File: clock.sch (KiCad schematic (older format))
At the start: 20 parts, among them SW2 SW_Push, SW3 SW_SPDT, U38 LM555xN, U39 74LS04, U40 74LS08, U41 74LS32, U42 LM555xN, U43 LM555xN

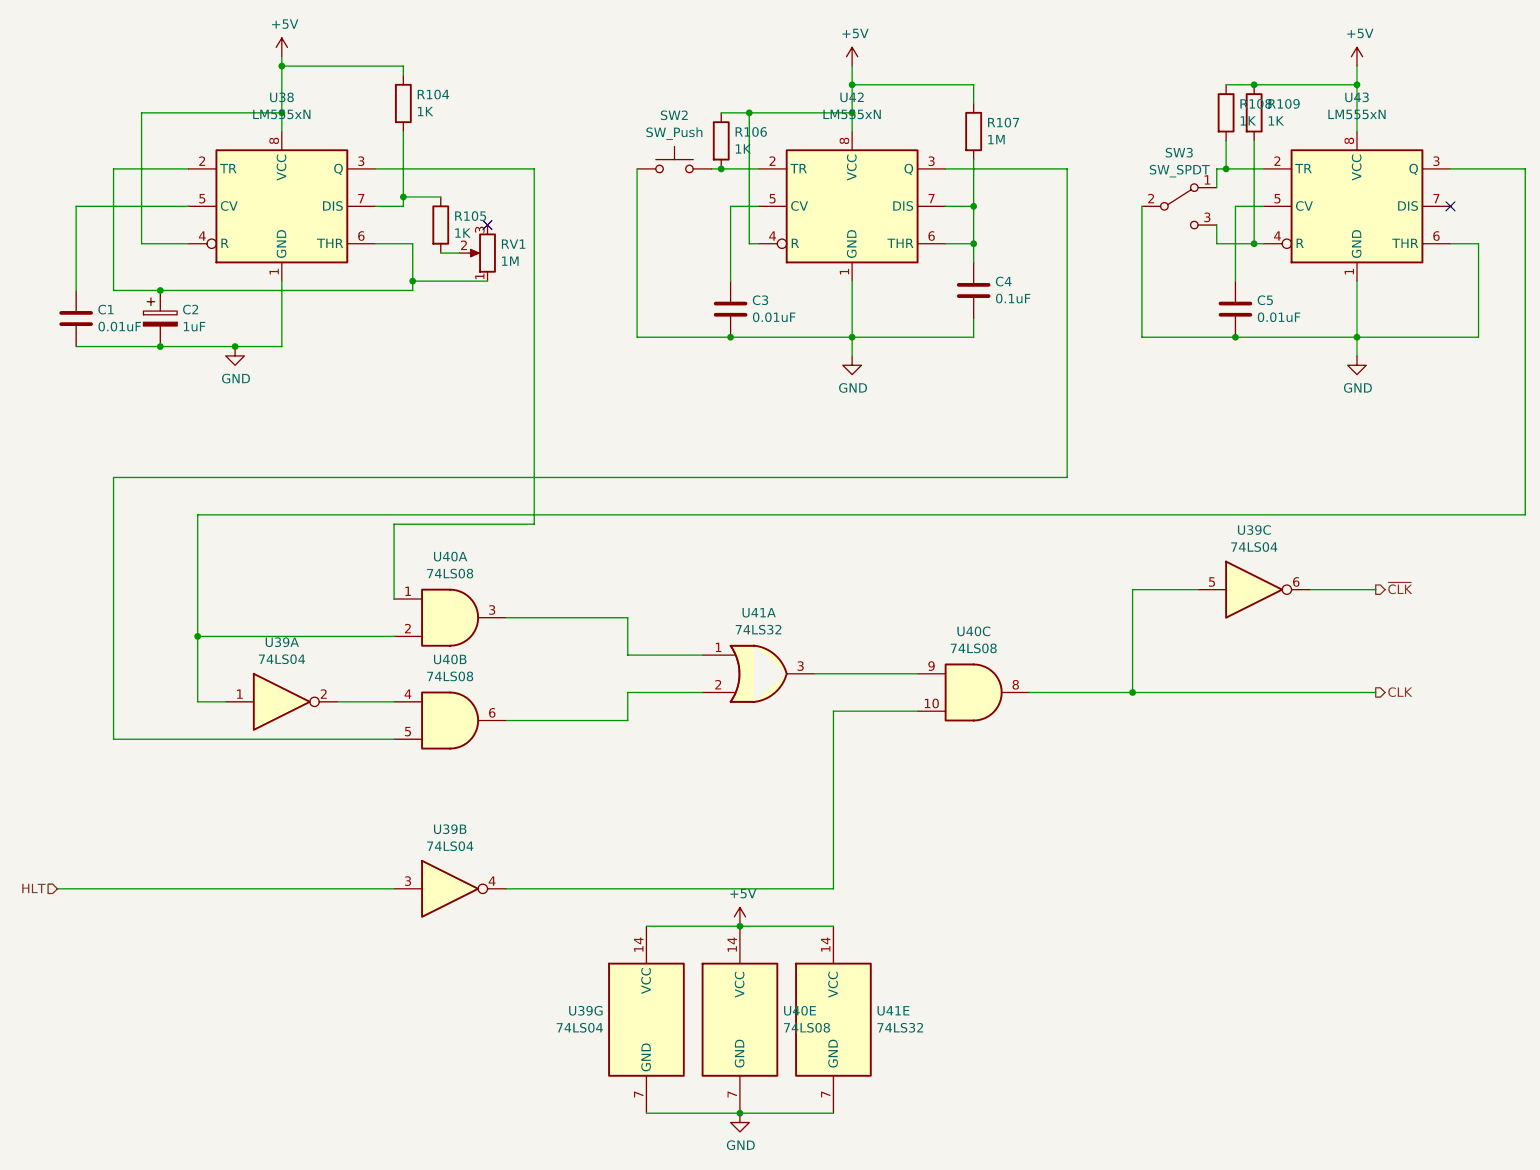
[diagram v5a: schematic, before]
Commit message: added timer.lib and using correct 555 timer
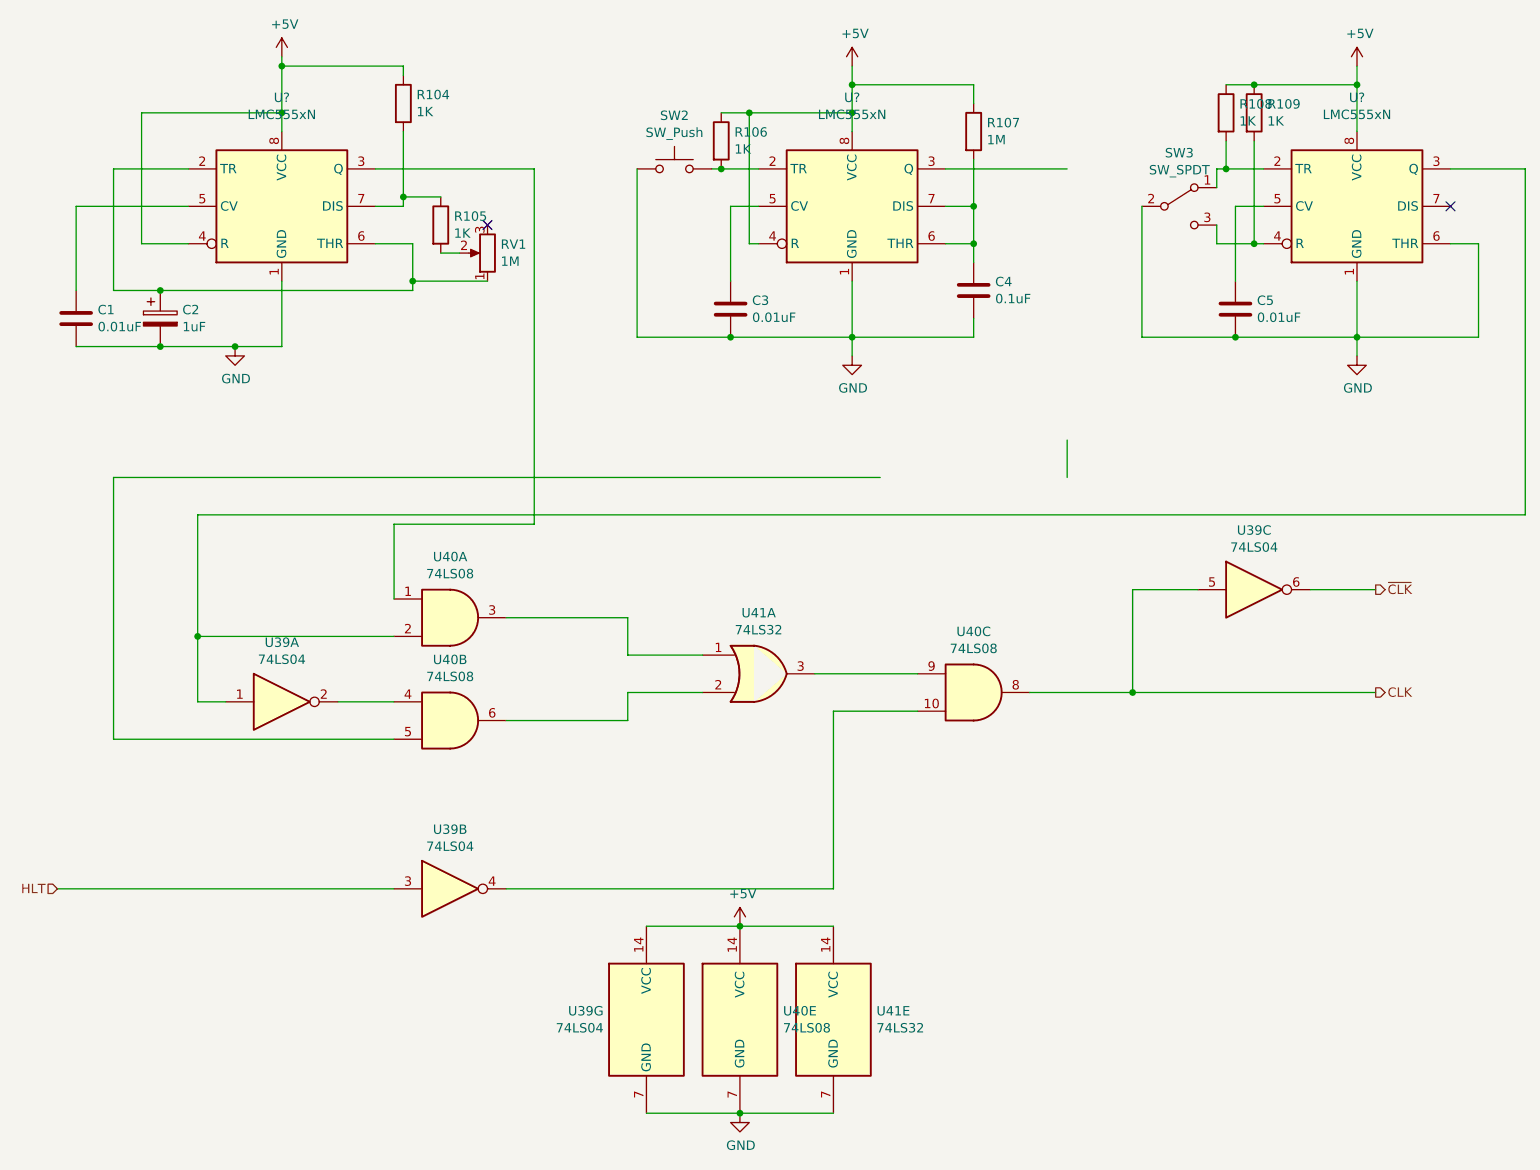
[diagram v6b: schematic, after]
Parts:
- removed U38, U42, U43: LM555xN, Package_DIP:DIP-8_W7.62mm, symbol 16bitCpu-rescue:LM555xN-Timer
- added U? (x3): LMC555xN, Package_DIP:DIP-8_W7.62mm, symbol Timer:LMC555xN
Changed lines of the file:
@@
 $Descr A4 11693 8268
 encoding utf-8
-Sheet 13 21
+Sheet 12 21
 Title ""
 Date ""
@@
 	9350 1700 9350 3550
 Wire Wire Line
-	9350 3550 2250 3550
-Wire Wire Line
 	2250 3550 2250 4200
 Wire Wire Line
@@
 	1800 4750 1800 3350
 Wire Wire Line
-	1800 3350 6900 3350
-Wire Wire Line
-	6900 3350 6900 1700
+	1800 3350 5900 3350
+Wire Wire Line
+	6900 3350 6900 3150
 Wire Wire Line
 	6900 1700 6250 1700
@@
 	1    0    0    -1
 $EndComp
-$Comp
-L 16bitCpu-rescue:LM555xN-Timer U?
-U 1 1 60AA52FF
+Wire Wire Line
+	1600 1900 1600 2350
+$Comp
+L Timer:LMC555xN U?
+U 1 1 5F9C497D
 P 2700 1900
-AR Path="/60AA52FF" Ref="U?"  Part="1"
-AR Path="/5F75E433/60AA52FF" Ref="U38"  Part="1"
-F 0 "U38" H 2700 2481 50  0000 C CNN
-F 1 "LM555xN" H 2700 2390 50  0000 C CNN
+F 0 "U?" H 2700 2481 50  0000 C CNN
+F 1 "LMC555xN" H 2700 2390 50  0000 C CNN
 F 2 "Package_DIP:DIP-8_W7.62mm" H 3350 1500 50  0001 C CNN
-F 3 "http://www.ti.com/lit/ds/symlink/lm555.pdf" H 3550 1500 50  0001 C CNN
+F 3 "" H 3550 1500 50  0001 C CNN
 	1    2700 1900
 	1    0    0    -1
 $EndComp
-Wire Wire Line
-	1600 1900 1600 2350
-$Comp
-L 16bitCpu-rescue:LM555xN-Timer U?
-U 1 1 60AB8137
+$Comp
+L Timer:LMC555xN U?
+U 1 1 5F9DBE25
 P 5750 1900
-AR Path="/60AB8137" Ref="U?"  Part="1"
-AR Path="/5F75E433/60AB8137" Ref="U42"  Part="1"
-F 0 "U42" H 5750 2481 50  0000 C CNN
-F 1 "LM555xN" H 5750 2390 50  0000 C CNN
+F 0 "U?" H 5750 2481 50  0000 C CNN
+F 1 "LMC555xN" H 5750 2390 50  0000 C CNN
 F 2 "Package_DIP:DIP-8_W7.62mm" H 6400 1500 50  0001 C CNN
-F 3 "http://www.ti.com/lit/ds/symlink/lm555.pdf" H 6600 1500 50  0001 C CNN
+F 3 "" H 6600 1500 50  0001 C CNN
 	1    5750 1900
 	1    0    0    -1
 $EndComp
-$Comp
-L 16bitCpu-rescue:LM555xN-Timer U?
-U 1 1 60AB9E78
+Wire Wire Line
+	2250 3550 9350 3550
+$Comp
+L Timer:LMC555xN U?
+U 1 1 5F9F76EE
 P 8450 1900
-AR Path="/60AB9E78" Ref="U?"  Part="1"
-AR Path="/5F75E433/60AB9E78" Ref="U43"  Part="1"
-F 0 "U43" H 8450 2481 50  0000 C CNN
-F 1 "LM555xN" H 8450 2390 50  0000 C CNN
+F 0 "U?" H 8450 2481 50  0000 C CNN
+F 1 "LMC555xN" H 8450 2390 50  0000 C CNN
 F 2 "Package_DIP:DIP-8_W7.62mm" H 9100 1500 50  0001 C CNN
-F 3 "http://www.ti.com/lit/ds/symlink/lm555.pdf" H 9300 1500 50  0001 C CNN
+F 3 "" H 9300 1500 50  0001 C CNN
 	1    8450 1900
 	1    0    0    -1
